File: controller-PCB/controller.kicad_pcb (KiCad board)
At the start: 2 copper layers, 38.1 x 54.1 mm, 24 parts, among them J1 Pinball I/O, J2 UART, J3 DOOR-IO, J4 DOOR-SW, Q1 NPN_BEC, Q2 NPN_BEC, Q3 NPN_BEC, Q4 NPN_BEC, Q5 NPN_BEC, Q6 NPN_BEC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

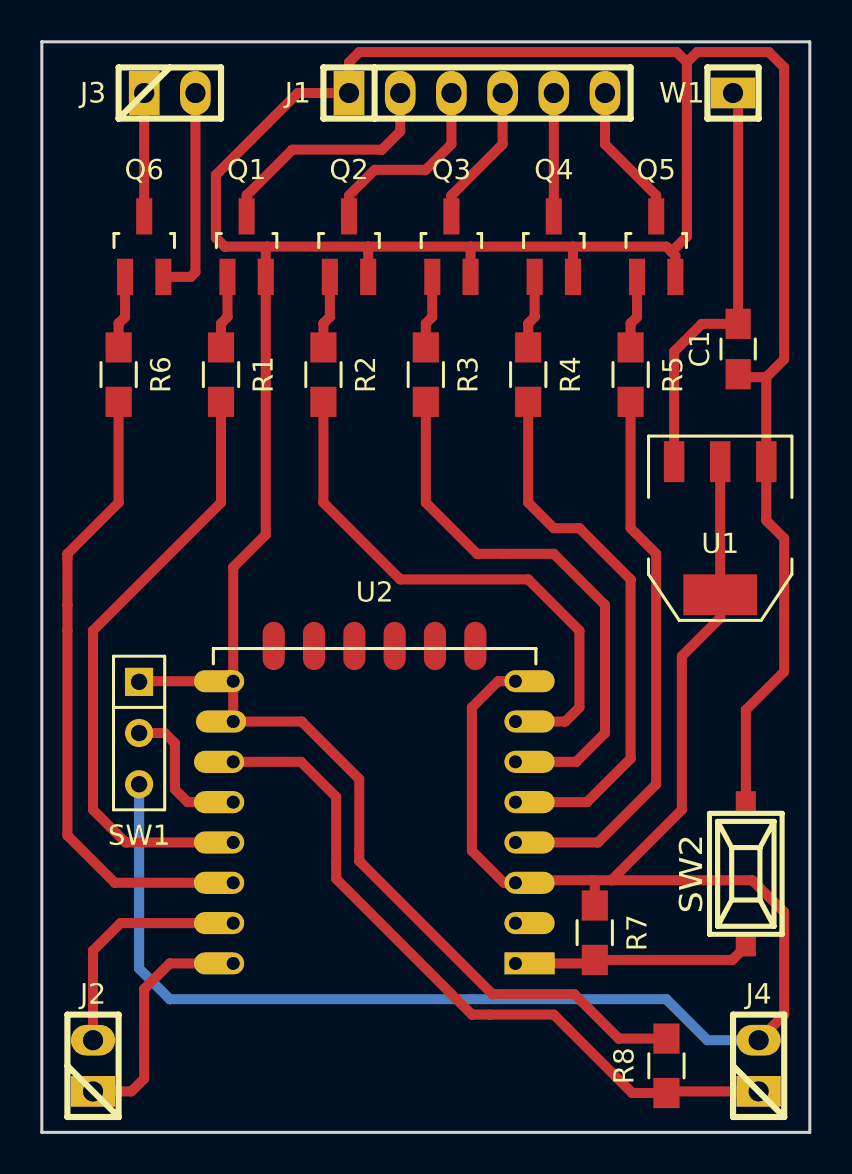
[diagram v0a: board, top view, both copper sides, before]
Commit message: Made the PCB design tighter and single layer
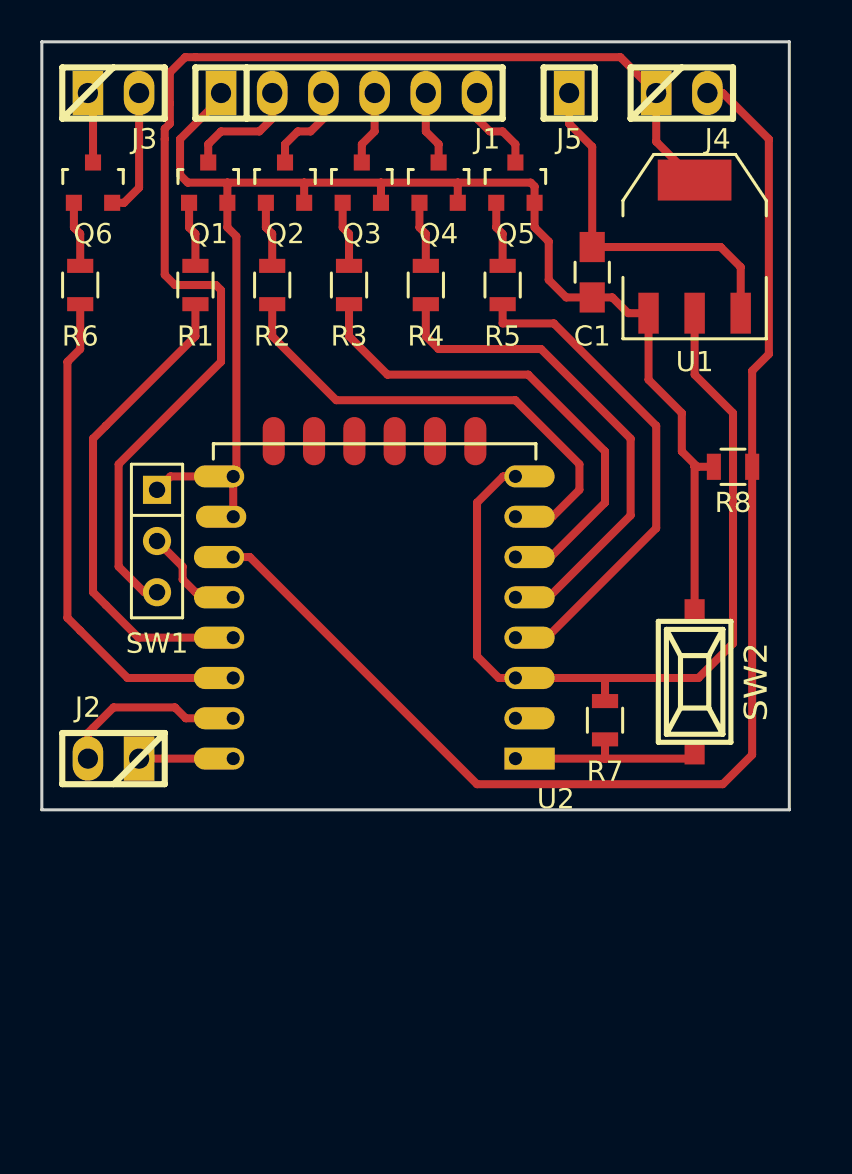
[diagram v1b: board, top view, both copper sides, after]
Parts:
- removed W1: 12V, w_pin_strip:pin_strip_1
- added J5: 12V, w_pin_strip:pin_strip_1, F.Cu at (26.2, 2.54)
- Q1, Q2, Q3, Q4, Q5, Q6: footprint TO_SOT_Packages_SMD:SOT-23_Handsoldering -> TO_SOT_Packages_SMD:SOT-23
- R1, R2, R3, R4, R5: value R -> 10; footprint Resistors_SMD:R_0805_HandSoldering -> Resistors_SMD:R_0805
- R6: footprint Resistors_SMD:R_0805_HandSoldering -> Resistors_SMD:R_0805
- R7, R8: value R -> 10k; footprint Resistors_SMD:R_0805_HandSoldering -> Resistors_SMD:R_0805
- moved J4 48.4 mm to (31.8, 2.54), turned to 0 degrees
- moved R8 29.9 mm to (34.3, 21.1), turned to 180 degrees
- moved J2 15.3 mm to (3.56, 35.6), turned to 180 degrees
- moved U1 14.0 mm to (32.4, 10.2), turned to 0 degrees
- moved R7 10.6 mm to (27.9, 33.7)
- moved U2 10.2 mm to (23.5, 35.6)
- moved SW2 9.86 mm to (32.4, 31.8)
- moved SW1 9.57 mm to (5.71, 24.8)
- moved C1 8.18 mm to (27.3, 11.4)
- moved R5 7.75 mm to (22.9, 12.1)
- moved Q5 7.67 mm to (23.5, 6.99)
- moved R4 6.75 mm to (19.1, 12.1)
- moved Q4 6.54 mm to (19.7, 6.99)
- moved J1 6.35 mm to (15.2, 2.54)
- moved R3 5.85 mm to (15.2, 12.1)
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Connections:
- J4 pad 1: DOOR-SW -> VCC
- J4 pad 2: VCC -> DOOR-SW
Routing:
- net GND: track 172.6 -> 74.1 mm
- net DOOR-SW: track 34.8 -> 65.9 mm
- net /TXD: track 12.2 -> 4.67 mm
- net Net-(R6-Pad2): track 32.2 -> 25.3 mm
- net Net-(R1-Pad2): track 30.9 -> 24.3 mm
- net /COIN: track 11.9 -> 5.88 mm
- net /Pinball-SW4: track 9.71 -> 4.61 mm
- net VCC: track 99.7 -> 104.1 mm
- net Net-(J3-Pad2): track 10.6 -> 6.34 mm
- net Net-(R2-Pad2): track 28.0 -> 24.5 mm
- net /Pinball-SW3: track 7.17 -> 3.71 mm
- net Net-(R5-Pad2): track 28.1 -> 25.0 mm
- net Net-(R3-Pad2): track 27.8 -> 24.8 mm
- net /RXD: track 12.0 -> 9.23 mm
- net +12V: track 20.8 -> 18.2 mm
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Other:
- board size 38.1 x 54.1 mm -> 37.1 x 38.1 mm
- net class Default: clearance 0.5 -> 0.35; trace_width 0.5 -> 0.4
- net class GND: clearance 0.1 -> 0.35; trace_width 0.5 -> 0.4
- net class Orange: clearance 0.5 -> 0.35; trace_width 0.5 -> 0.4
- net class VCC: clearance 0.5 -> 0.35; trace_width 0.5 -> 0.4
- rule trace_clearance: 0.5 -> 0.35

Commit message: Made some minor changes to the PCB design and schematic.
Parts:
- moved R4 0.28 mm to (18.8, 12.2)
- moved R1 0.28 mm to (7.37, 12.2)
- moved R2 0.28 mm to (11.2, 12.2)
- moved R3 0.28 mm to (15.0, 12.2)
- moved R5 0.28 mm to (22.6, 12.2)

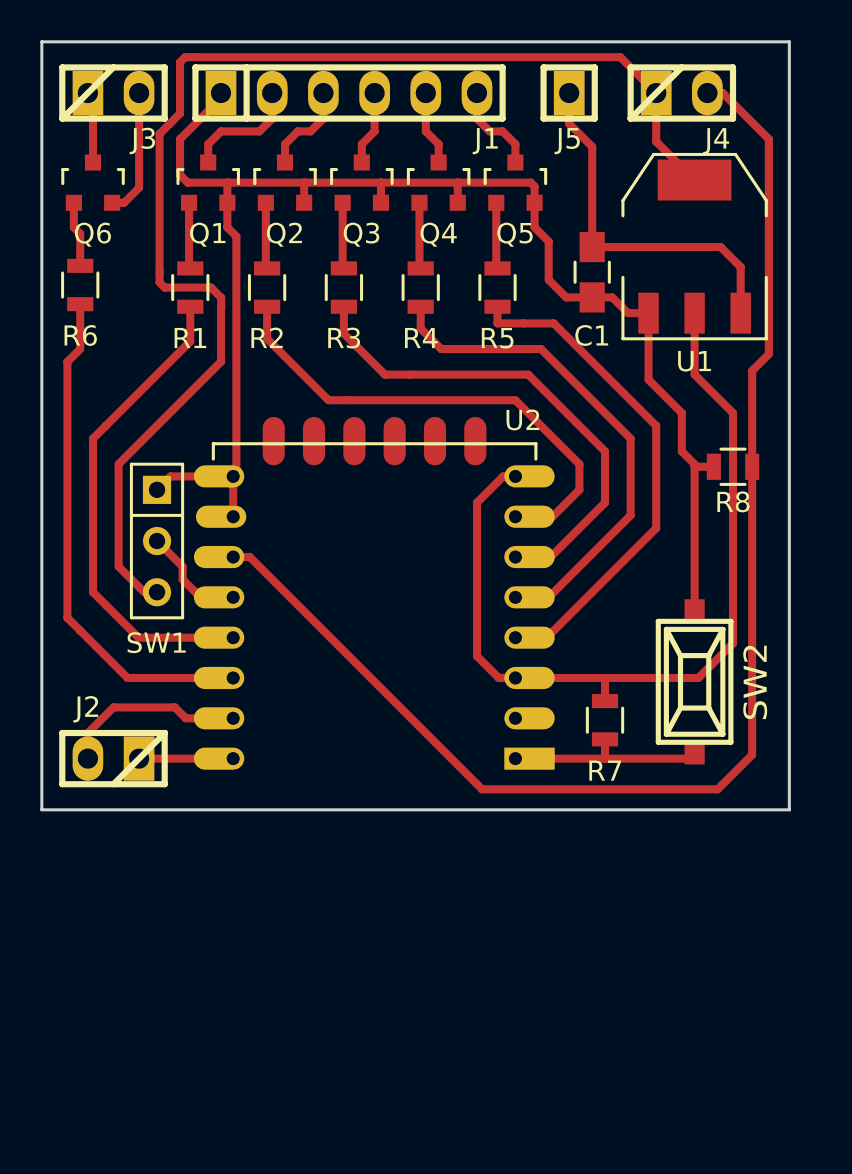
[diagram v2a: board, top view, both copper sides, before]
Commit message: Corrected the values of the regulator capacitors and added one on the output.
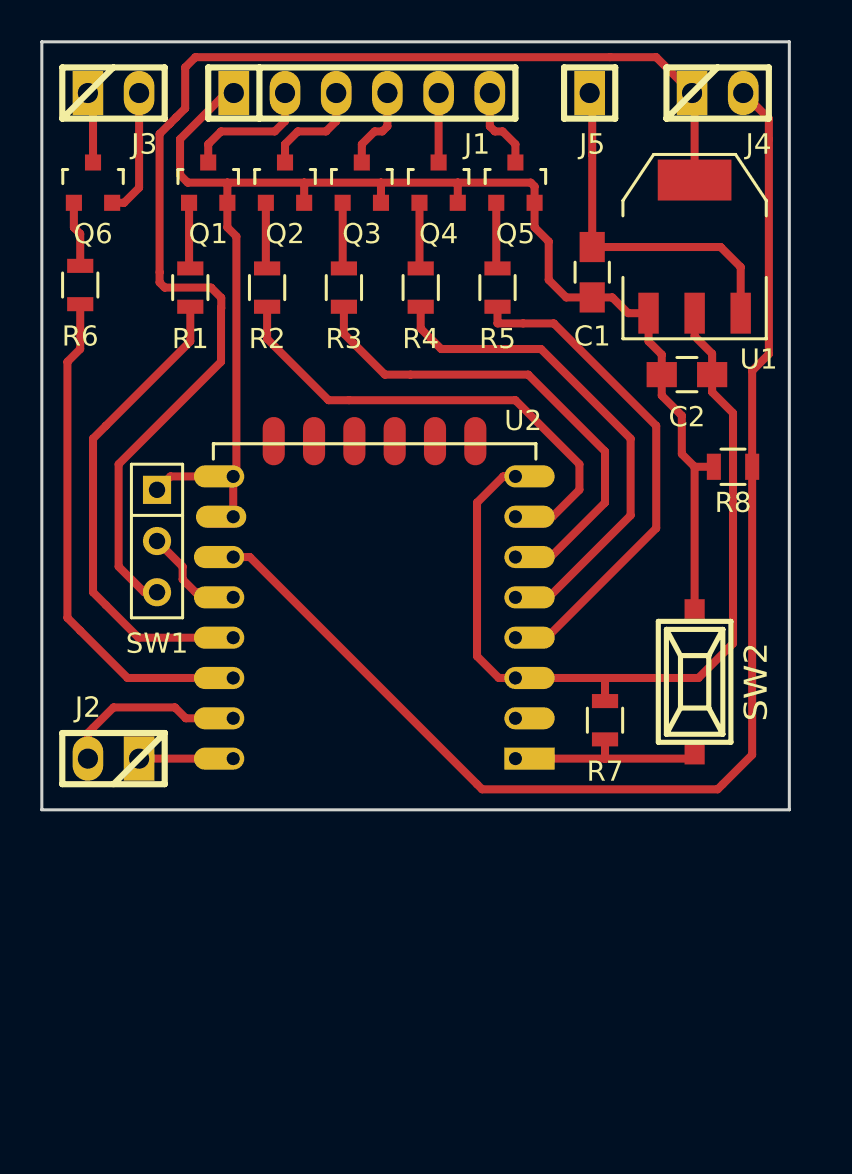
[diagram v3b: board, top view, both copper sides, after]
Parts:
- added C2: 10uF, Capacitors_SMD:C_0805_HandSoldering, F.Cu at (32.0, 16.5)
- C1: value 4.7uF -> 10uF
- R1, R2, R3, R4, R5: value 10 -> 1kΩ
- R6: value R -> 1kΩ
- R7, R8: value 10k -> 10kΩ
- moved J4 1.78 mm to (33.5, 2.54)
- moved J5 1.02 mm to (27.2, 2.54)
- moved J1 0.63 mm to (15.9, 2.54)
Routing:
- net DOOR-SW: track 66.1 -> 64.9 mm
- net VCC: track 104.4 -> 105.2 mm
- net /Pinball-SW4: track 4.61 -> 5.32 mm
- net /COIN: track 5.88 -> 6.59 mm
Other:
- board text added: "+12V"
- board text added: "DOOR+ DOOR-"
- board text added: "FLASH-BOOT"
- board text added: "GND COIN SW4 SW3 SW2 SW1"
- board text added: "RX TX"
- board text added: "SW ROW 2 SW COL 2"
